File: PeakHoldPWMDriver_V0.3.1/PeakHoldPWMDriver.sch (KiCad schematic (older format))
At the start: 120 parts, among them J1 RND 205-00203, J2 RND 205-00205, Q1 2N7002, Q10 2N7002, Q11 2N7002, Q12 2N7002, Q13 TSM2309, Q14 IRLL 024N, Q15 TSM2309, Q16 IRLL 024N, Q17 TSM2309, Q18 TSM2309, Q19 TSM2309, Q2 2N7002, Q20 TSM2309, Q3 2N7002, Q4 2N7002, Q5 TSM2309, Q6 TSM2309, Q7 IRLL 024N, Q8 IRLL 024N, Q9 2N7002, U1 74LS32, U2 LM2901, U3 74LS74, U4 LTC6992, U5 74LS74, U6 LM340, U7 74LS08, U8 74LS08, U9 LM2904

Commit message: updates values on 0.3 added 0.3.1
Updated resistor values for V0.3
Added V0.3.1 with new battery voltage compensation
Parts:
- removed C9: 220nf, Capacitor_SMD:C_0603_1608Metric_Pad1.05x0.95mm_HandSolder, symbol Speeduino_base-eagle-import:CERAMIC-220NF-25V-10%-X7R(0603)
- removed R1: 15k, Resistor_SMD:R_0603_1608Metric, symbol Device:R_Small
- removed R46: 9.1k, Resistor_SMD:R_0603_1608Metric, symbol Device:R_Small
- removed U9: LM2904, Package_SO:SO-8_3.9x4.9mm_P1.27mm, symbol Amplifier_Operational:LM2904
- R11, R28, R44: value 1K -> 10K
- R12, R29: value 1K -> 470R
- R4: value 12k -> 100k
- R45: value 91k -> 120k
- R47: value 6.2k -> 33k
- R5: value 100k -> 28k
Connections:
- wire segments 367 -> 357
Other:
- moved on the sheet: R45, R47, RV2

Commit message: Update parts V0.3.1
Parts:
- U1: value 74LS32 -> 74HC32
- U3, U5: value 74LS74 -> 74HC74
- U7, U8: value 74LS08 -> 74HC08

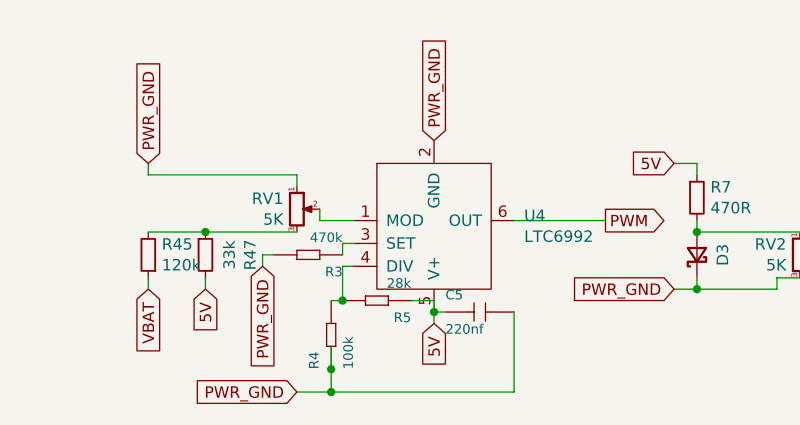
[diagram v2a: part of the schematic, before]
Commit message: Changed resistor value R5, now correct PWM freqency
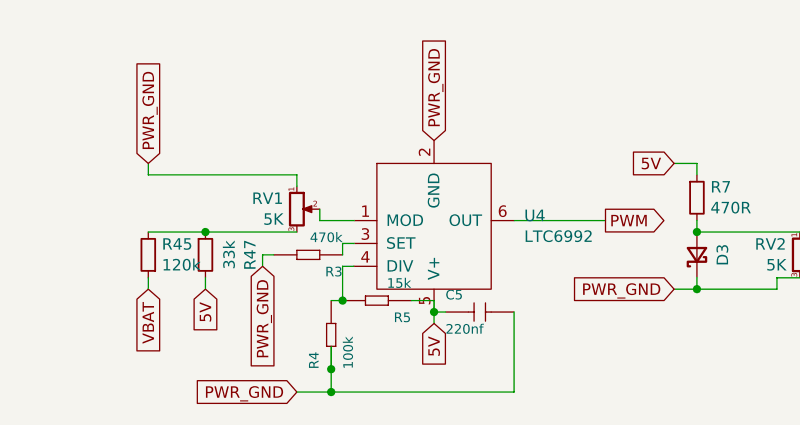
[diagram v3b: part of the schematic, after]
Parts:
- R5: value 28k -> 15k
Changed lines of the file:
@@
 P 2050 6950
 F 0 "R5" H 1900 7000 42  0000 L BNN
-F 1 "28k" H 1900 6850 42  0000 L BNN
+F 1 "15k" H 1900 6850 42  0000 L BNN
 F 2 "Resistor_SMD:R_0603_1608Metric_Pad1.05x0.95mm_HandSolder" H 2050 6950 50  0001 C CNN
 F 3 "" H 2050 6950 50  0001 C CNN

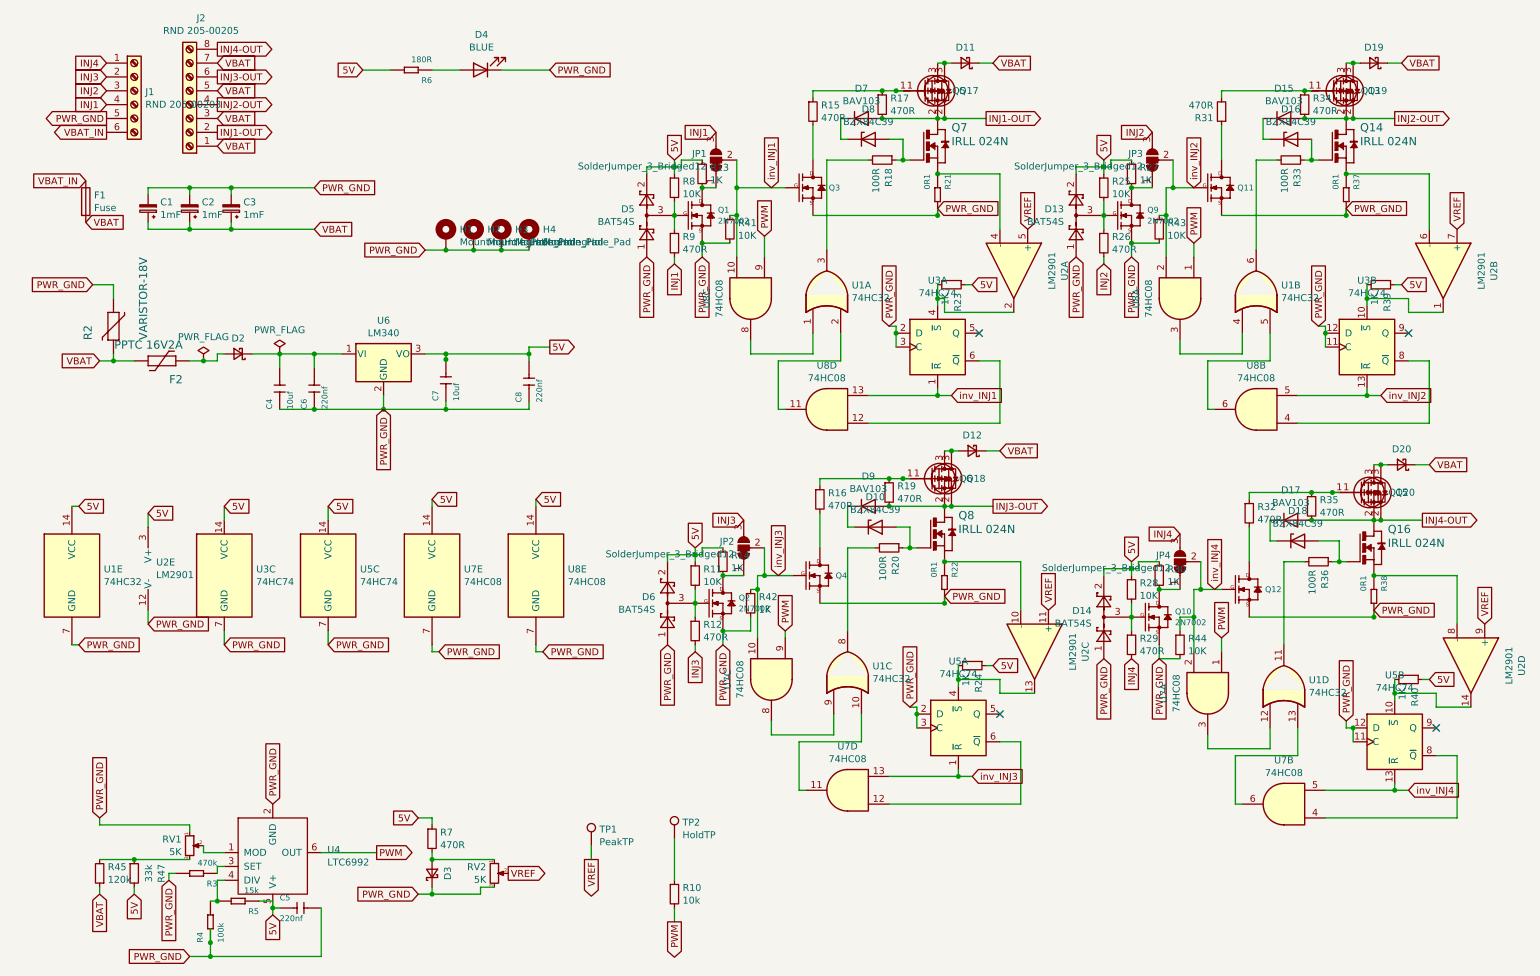
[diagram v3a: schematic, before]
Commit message: Update schematic for clarity
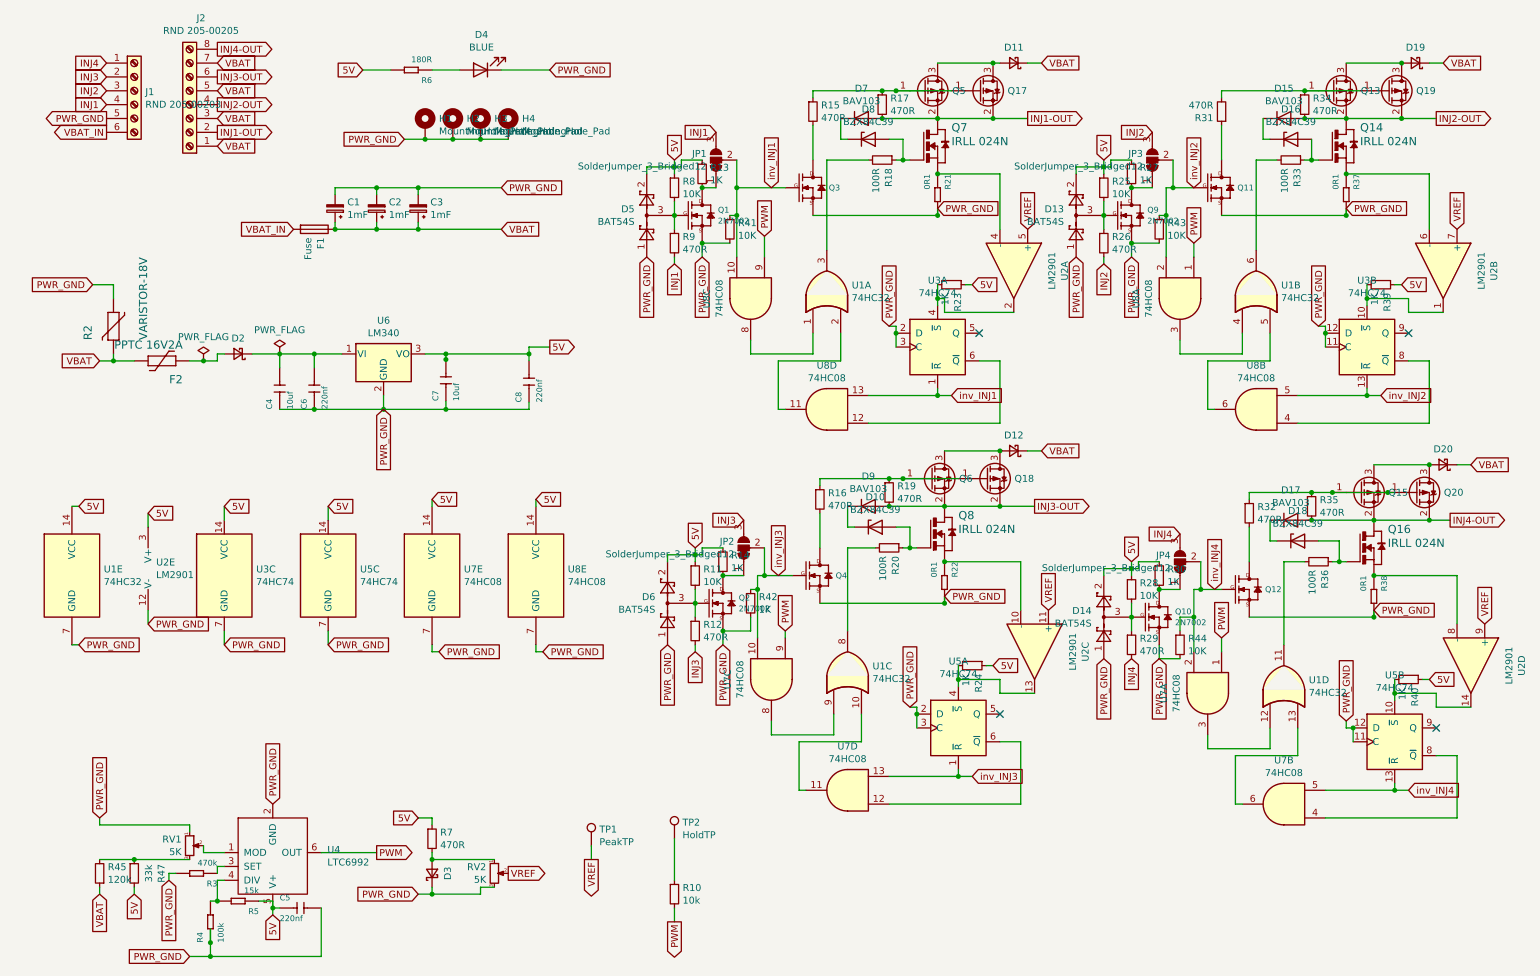
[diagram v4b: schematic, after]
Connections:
- net VBAT: now also F1.1; no longer F1.2
- net VBAT_IN: now also F1.2; no longer F1.1
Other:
- moved on the sheet: C1, C2, C3, D11, D12, D19, D20, F1, H1, H2, H3, H4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
